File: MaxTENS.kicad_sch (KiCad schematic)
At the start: 18 parts, among them J2 54-00170, J3 54-00170, J6 Conn_01x02_Pin

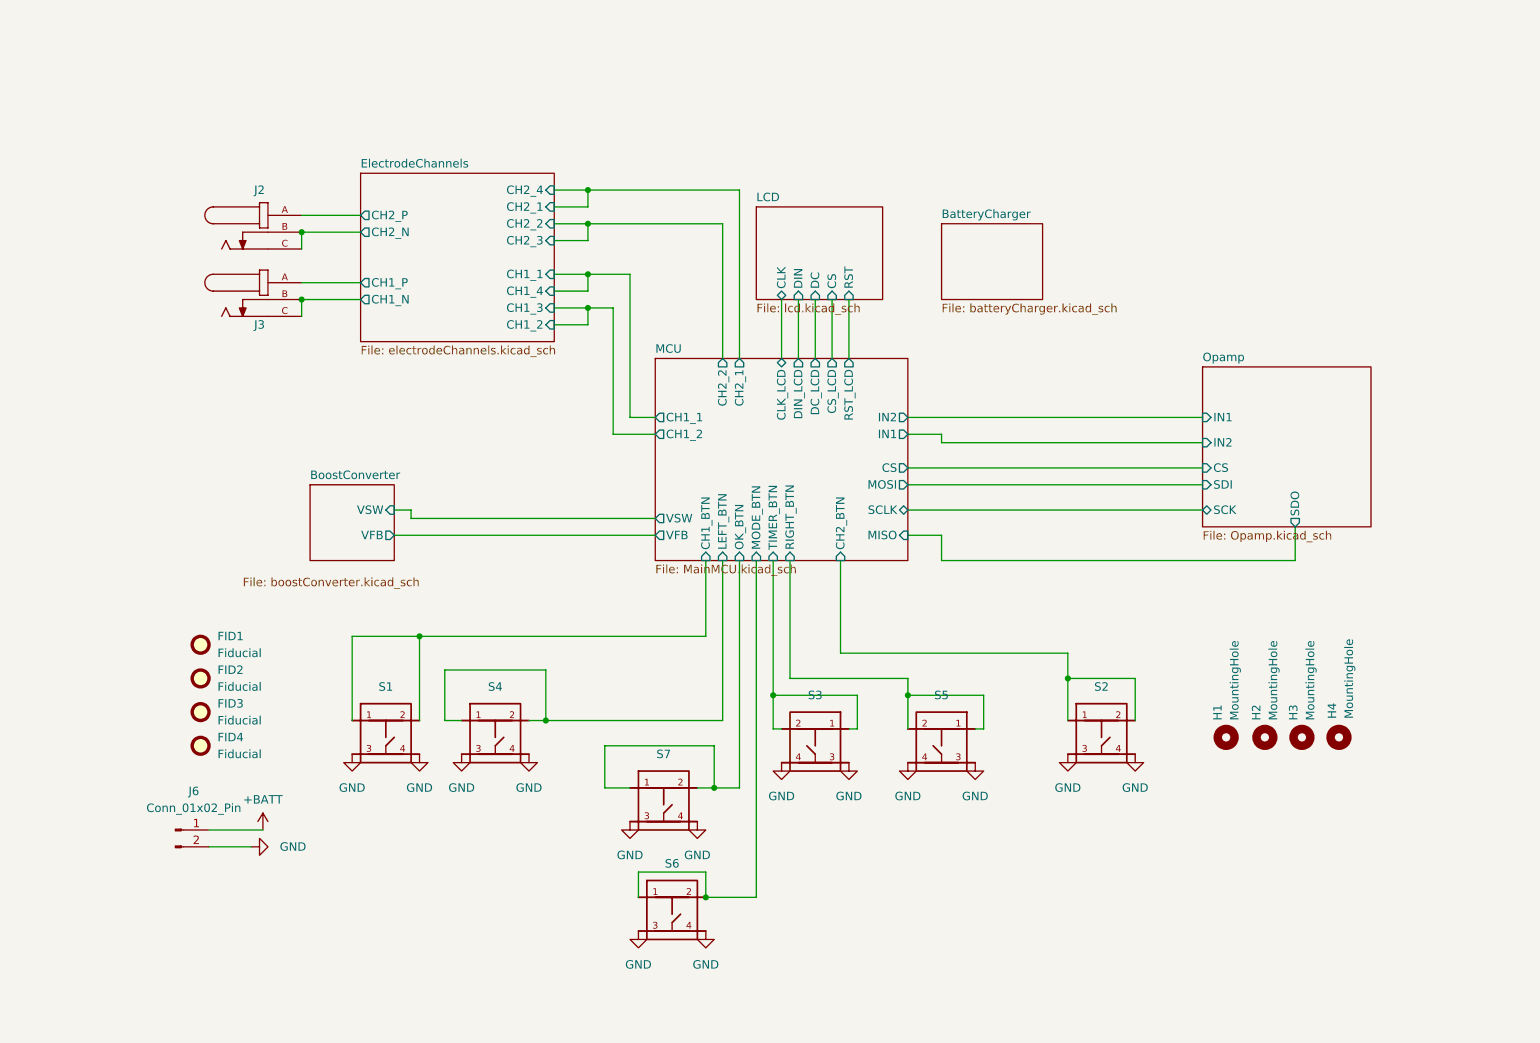
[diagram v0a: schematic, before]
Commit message: version 2 with 0.8mm thickness
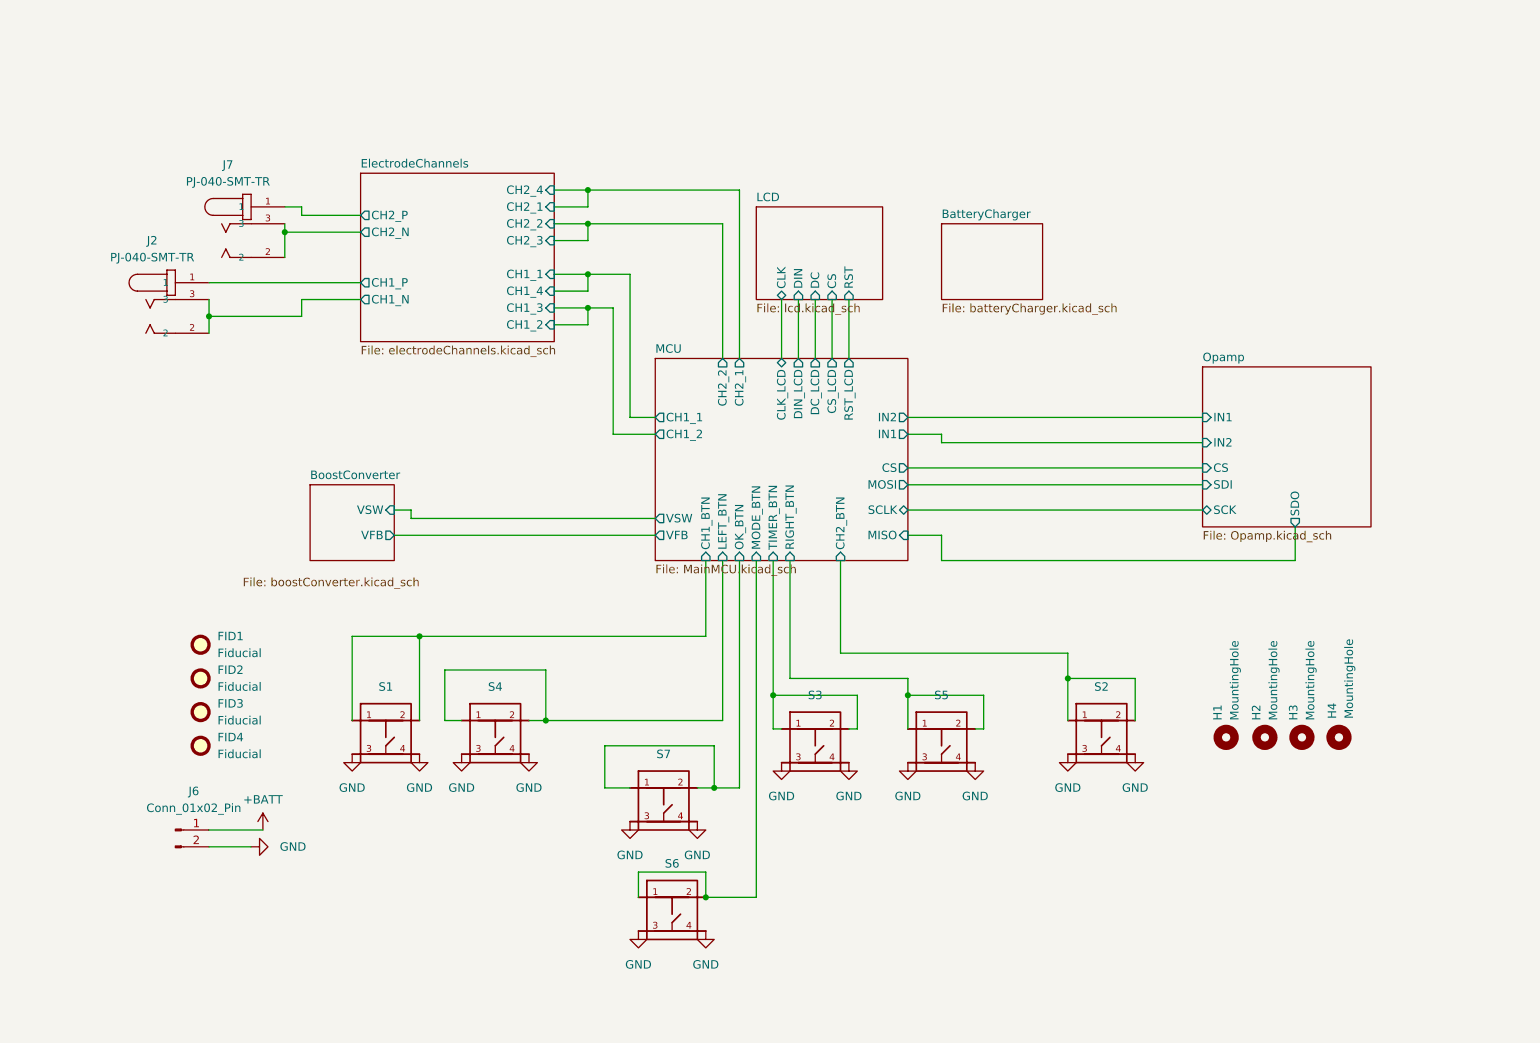
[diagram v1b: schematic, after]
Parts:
- removed J2, J3: 54-00170, Library:TENSILITY_54-00170, symbol 2023-09-03_14-36-57:54-00170
- added J2, J7: PJ-040-SMT-TR, Library:CUI_PJ-040-SMT-TR, symbol 2023-09-03_14-36-57:PJ-040-SMT-TR
- S1, S2, S3, S4, S5, S6, S7: value PTS647SM38SMTR2LFS -> PTS815 SJM 250 SMTR LFS; footprint Library:SW_PTS647SM38SMTR2LFS_CNK -> Library:SW4_PTS815 SJM 250 SMTR LFS_CNK; Manufacturer Part Number PTS647SM38SMTR2LFS -> PTS815 SJM 250 SMTR LFS
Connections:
- net ElectrodeChannels/CH1_N: now also J2.2, J2.3
- net ElectrodeChannels/CH1_P: now also J2.1
- net ElectrodeChannels/CH2_N: now also J7.2, J7.3
- net ElectrodeChannels/CH2_P: now also J7.1

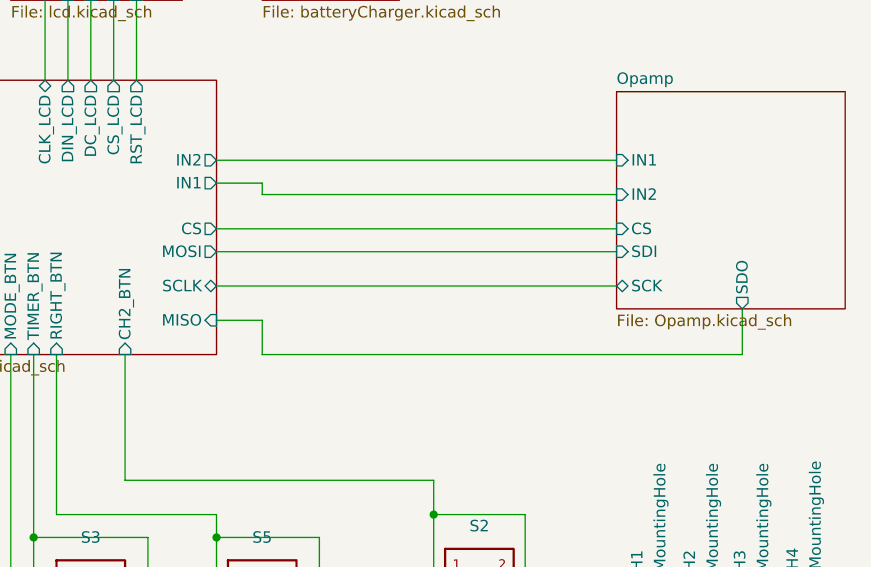
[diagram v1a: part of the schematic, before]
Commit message: v3: removed digital potentiometer, added 8 discrete resistors and one GPIO expander
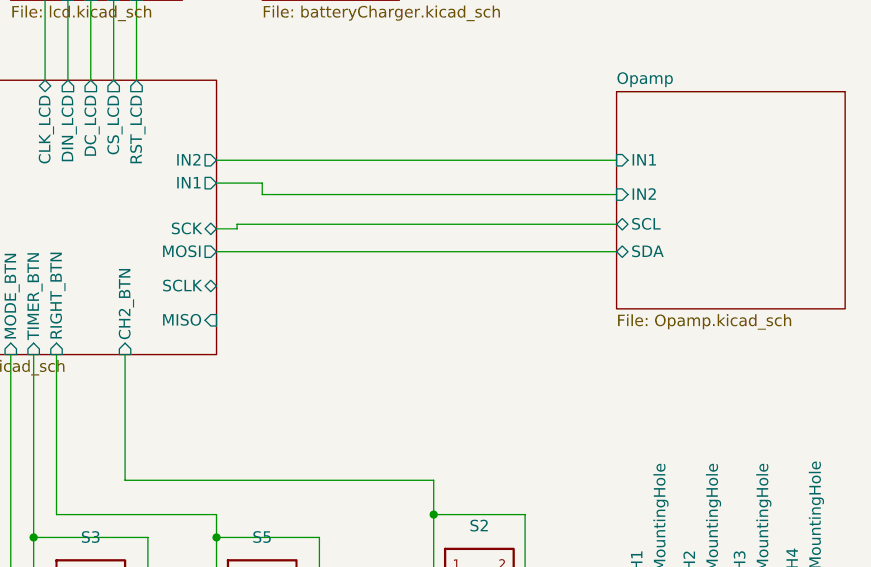
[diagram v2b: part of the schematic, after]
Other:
- sheet MCU ports: added SCK; removed CS
- sheet Opamp ports: added SCL, SDA; removed CS, SCK, SDI, SDO
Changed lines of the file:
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@@
     (stroke (width 0) (type default))
   )
-  (wire (pts (xy 191.77 97.79) (xy 191.77 101.6))
+  (wire (pts (xy 186.69 87.63) (xy 188.976 87.63))
     (stroke (width 0) (type default))
   )
@@
     (stroke (width 0) (type default))
   )
-  (wire (pts (xy 186.69 93.98) (xy 231.14 93.98))
-    (stroke (width 0) (type default))
-  )
   (wire (pts (xy 210.82 119.38) (xy 210.82 125.73))
     (stroke (width 0) (type default))
@@
     (stroke (width 0) (type default))
   )
-  (wire (pts (xy 186.69 87.63) (xy 231.14 87.63))
-    (stroke (width 0) (type default))
-  )
   (wire (pts (xy 140.97 129.54) (xy 157.48 129.54))
     (stroke (width 0) (type default))
@@
     (stroke (width 0) (type default))
   )
-  (wire (pts (xy 186.69 97.79) (xy 191.77 97.79))
-    (stroke (width 0) (type default))
-  )
   (wire (pts (xy 81.28 62.23) (xy 81.28 64.77))
     (stroke (width 0) (type default))
@@
     (stroke (width 0) (type default))
   )
-  (wire (pts (xy 245.11 101.6) (xy 245.11 96.52))
-    (stroke (width 0) (type default))
-  )
   (wire (pts (xy 158.75 50.8) (xy 158.75 71.12))
     (stroke (width 0) (type default))
@@
     (stroke (width 0) (type default))
   )
-  (wire (pts (xy 191.77 101.6) (xy 245.11 101.6))
+  (wire (pts (xy 188.976 87.122) (xy 231.14 87.122))
     (stroke (width 0) (type default))
   )
@@
   )
   (wire (pts (xy 133.35 50.8) (xy 138.43 50.8))
+    (stroke (width 0) (type default))
+  )
+  (wire (pts (xy 188.976 87.63) (xy 188.976 87.122))
     (stroke (width 0) (type default))
   )
@@
       (effects (font (size 1.27 1.27)) (justify left top))
     )
-    (pin "SDO" output (at 245.11 96.52 270)
-      (effects (font (size 1.27 1.27)) (justify left))
-    )
-    (pin "CS" input (at 231.14 87.63 180)
-      (effects (font (size 1.27 1.27)) (justify left))
-    )
-    (pin "SCK" bidirectional (at 231.14 93.98 180)
-      (effects (font (size 1.27 1.27)) (justify left))
-    )
-    (pin "SDI" input (at 231.14 90.17 180)
-      (effects (font (size 1.27 1.27)) (justify left))
-    )
     (pin "IN1" input (at 231.14 80.01 180)
       (effects (font (size 1.27 1.27)) (justify left))
     )
     (pin "IN2" input (at 231.14 83.82 180)
+      (effects (font (size 1.27 1.27)) (justify left))
+    )
+    (pin "SDA" bidirectional (at 231.14 90.17 180)
+      (effects (font (size 1.27 1.27)) (justify left))
+    )
+    (pin "SCL" bidirectional (at 231.14 87.122 180)
       (effects (font (size 1.27 1.27)) (justify left))
     )
@@
       (effects (font (size 1.27 1.27)) (justify right))
     )
-    (pin "CS" output (at 186.69 87.63 0)
-      (effects (font (size 1.27 1.27)) (justify right))
-    )
+    (pin "SCK" bidirectional (at 186.69 87.63 0)
+      (effects (font (size 1.27 1.27)) (justify right))
+    )

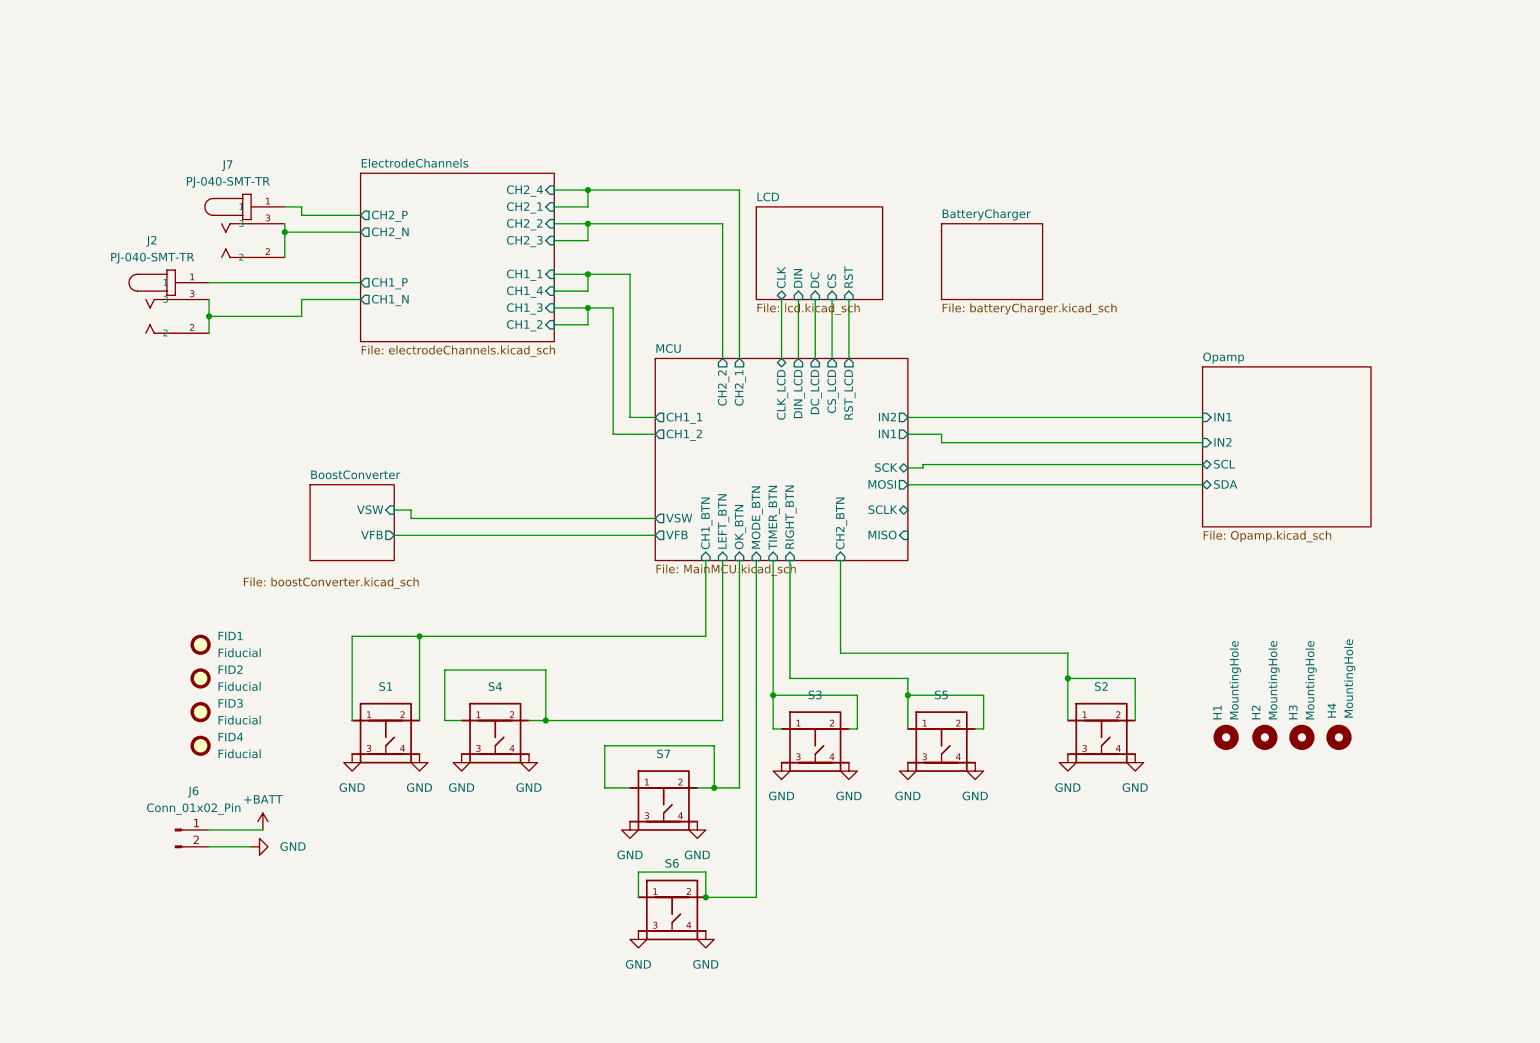
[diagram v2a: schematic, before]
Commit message: version 4: changed GPIO expander, added current sense resistor to electrodes, added buzzer pins, fixed some gpio inputs that needs to be pulled high, added battery charge detection, added battery level measurement feature
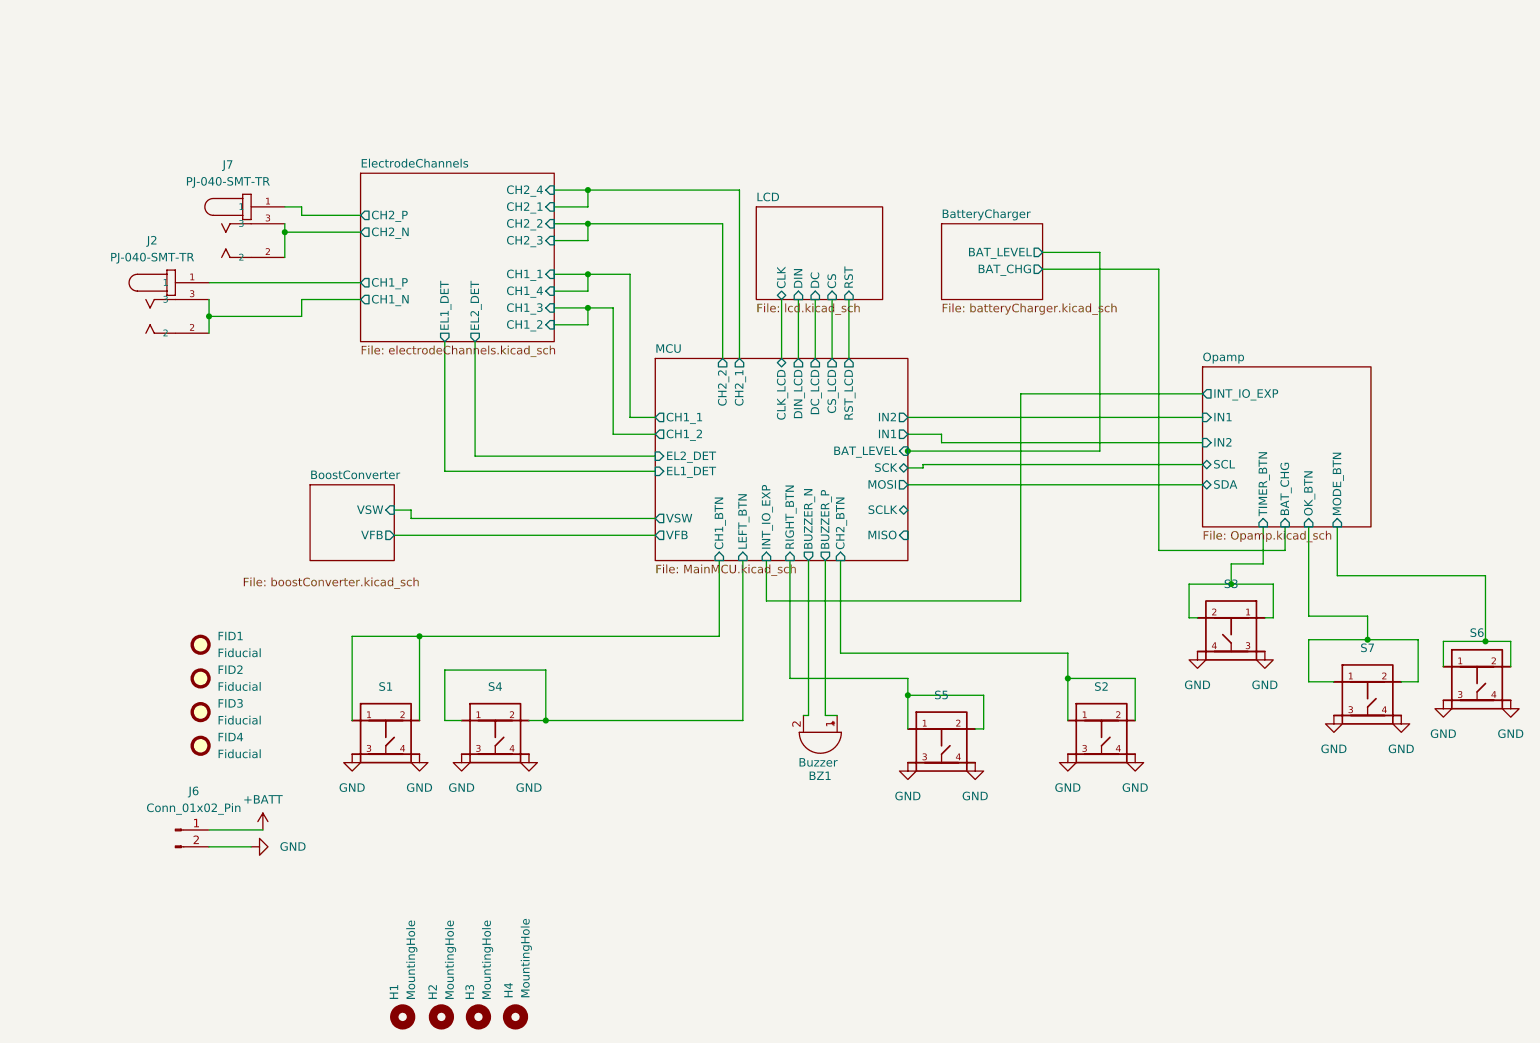
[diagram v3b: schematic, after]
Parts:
- added BZ1: Buzzer, Connector_PinHeader_2.54mm:PinHeader_1x02_P2.54mm_Vertical, symbol Device:Buzzer
- FID1, FID2, FID3, FID4, H1, H2, H3, H4: Long Description (none) -> DNP; Manufacturer (none) -> N/A; Manufacturer Part Number (none) -> N/A
- J6: Long Description (none) -> 505060 Battery 2000mA
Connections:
- net MCU/MODE_BTN renamed Opamp/MODE_BTN
- net MCU/OK_BTN renamed Opamp/OK_BTN
- net MCU/TIMER_BTN renamed Opamp/TIMER_BTN
- new net MCU/BUZZER_N: BZ1.2 (+)
- new net MCU/BUZZER_P: BZ1.1 (-)
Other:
- sheet BatteryCharger ports: added BAT_CHG, BAT_LEVEL; removed none
- sheet ElectrodeChannels ports: added EL1_DET, EL2_DET; removed none
- sheet MCU ports: added BAT_LEVEL, BUZZER_N, BUZZER_P, EL1_DET, EL2_DET, INT_IO_EXP; removed MODE_BTN, OK_BTN, TIMER_BTN
- sheet Opamp ports: added BAT_CHG, INT_IO_EXP, MODE_BTN, OK_BTN, TIMER_BTN; removed none
- moved on the sheet: H1, H2, H3, H4, S3, S6, S7
